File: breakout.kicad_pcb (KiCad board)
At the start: 2 copper layers, 26 x 23.8 mm, 11 parts, among them P1 CONN_01X09, P2 CONN_01X09, U1 ESP-12E, U2 APE8865Y5-33-HF-3

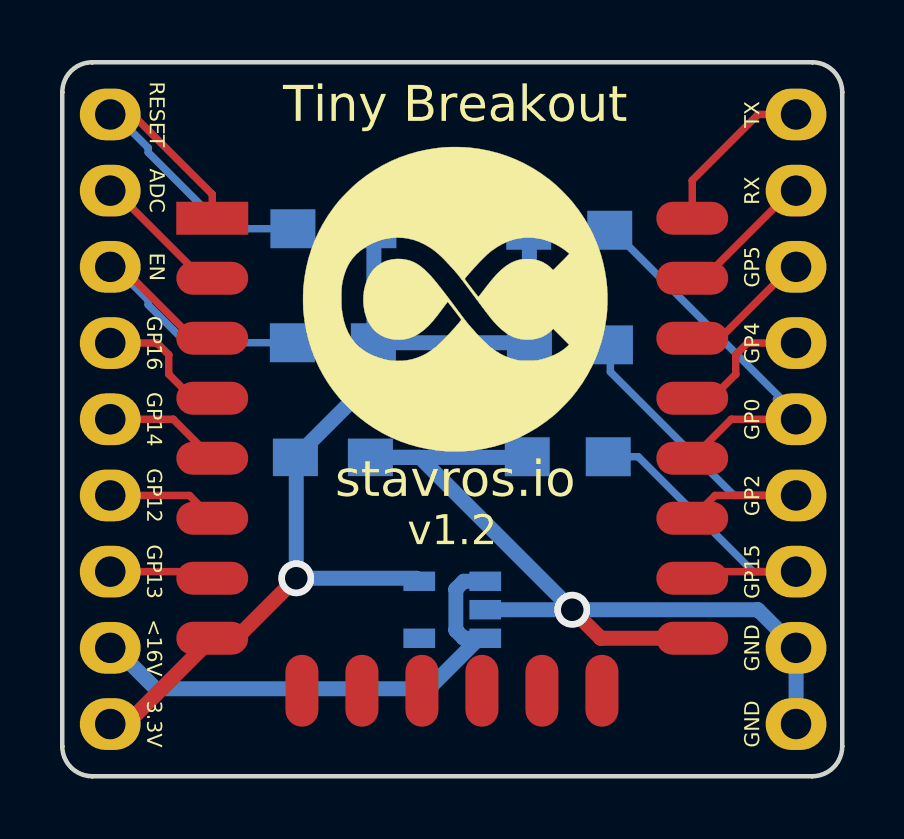
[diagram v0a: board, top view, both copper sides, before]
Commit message: Change to HT7333 regulator.
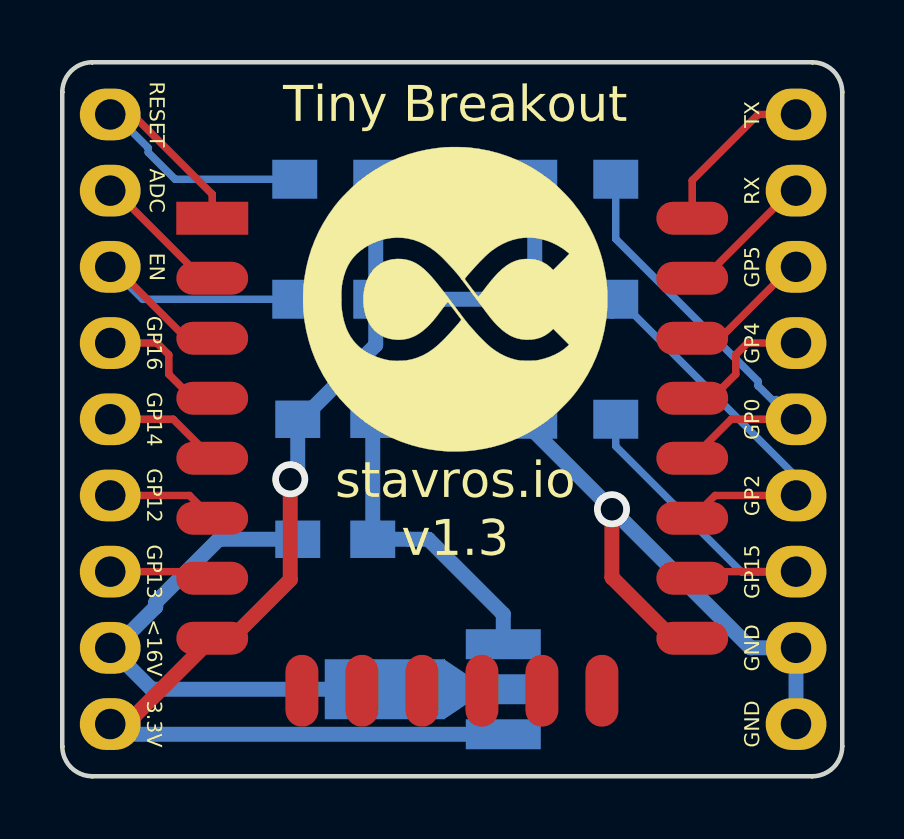
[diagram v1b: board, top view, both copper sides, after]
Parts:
- added C2: 10uF, Capacitors_SMD:C_0805_HandSoldering, B.Cu at (134.5, 67.5)
- C1: value 1uF -> 10uF
- U2: value APE8865Y5-33-HF-3 -> HT7333; footprint SOT-23-5 -> TO_SOT_Packages_SMD:SOT89-3_Housing_Handsoldering
- moved U2 2.73 mm to (137.8, 72.5), turned to 270 degrees
- moved R6 1.71 mm to (142.5, 55.5)
- moved R2 1.65 mm to (134.5, 55.5)
- moved R4 1.53 mm to (142.5, 59.5)
- moved R1 1.45 mm to (134.5, 59.5)
- moved R3 1.27 mm to (142.5, 63.5)
- moved C1 1.27 mm to (134.5, 63.5)
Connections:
- U2 pad 1: +12V -> GND
- U2 pad 2: GND -> /3V3
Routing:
- net /3V3: track 34.2 -> 50.4 mm
- net +12V: track 17.5 -> 23.1 mm
- net GND: track 31.9 -> 36.3 mm
- net Net-(P2-Pad5): track 13.9 -> 15.7 mm
- net Net-(P2-Pad7): track 11.4 -> 12.2 mm
- net Net-(P1-Pad1): track 13.1 -> 12.4 mm
- net Net-(P1-Pad3): track 11.6 -> 11.0 mm
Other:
- board text added: "stavros.io v1.3"
- board text removed: "C1"
- board text removed: "R1"
- board text removed: "R2"
- board text removed: "R3"
- board text removed: "R4"
- board text removed: "R6"
- board text removed: "stavros.io"
- board text removed: "v1.2"

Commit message: Switch back to the SPX regulator.
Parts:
- removed G***: LOGO, Stochastic:Logo_10mm
- U2: value HT7333 -> SPX3819M5-L-3-3; footprint TO_SOT_Packages_SMD:SOT89-3_Housing_Handsoldering -> TO_SOT_Packages_SMD:SOT-23-5
- moved U2 0.90 mm to (138.5, 72.0), turned to 180 degrees
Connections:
- U2 pad 1: GND -> +12V
- U2 pad 2: /3V3 -> GND
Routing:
- net GND: track 36.3 -> 43.8 mm
- net +12V: track 23.1 -> 19.2 mm
- net /3V3: track 50.4 -> 49.2 mm
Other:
- board text added: "stavros.io v1.4"
- board text removed: "stavros.io v1.3"

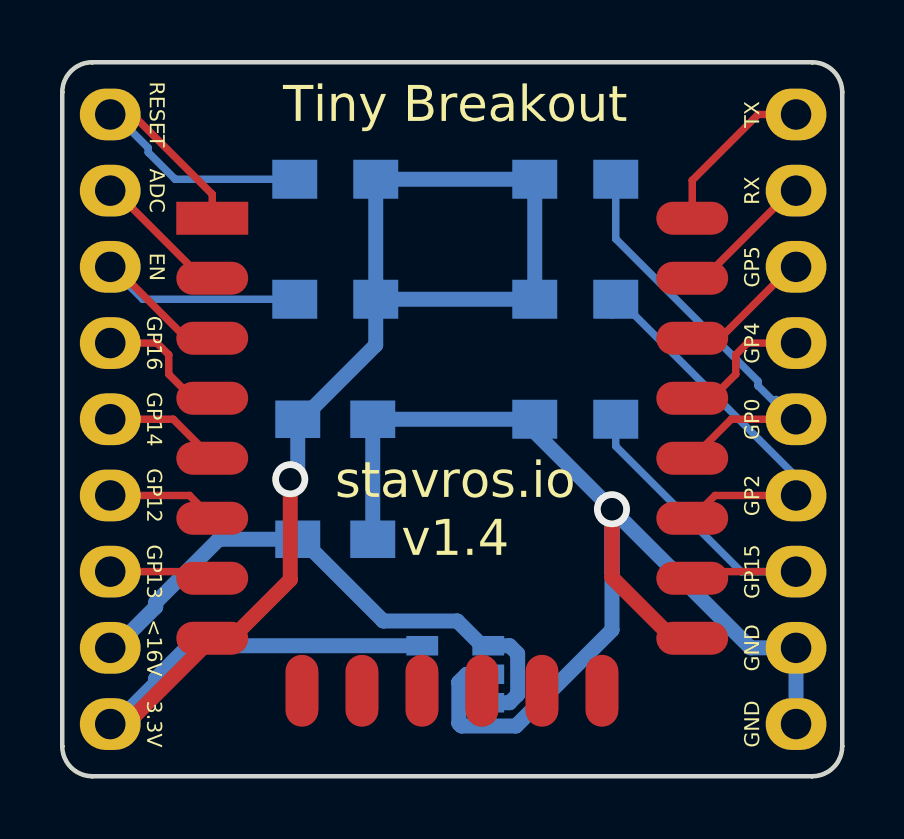
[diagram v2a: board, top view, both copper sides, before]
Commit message: Make PCB a bit smaller.
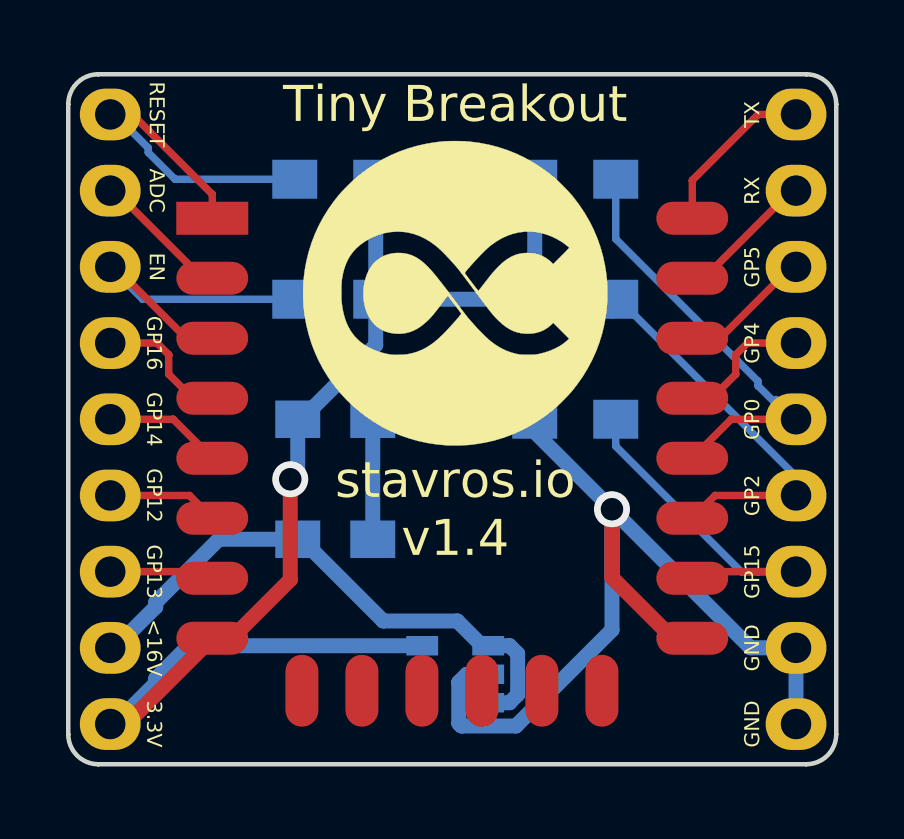
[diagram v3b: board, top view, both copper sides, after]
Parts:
- added G***: LOGO, Stochastic:Logo_10mm, F.Cu at (138.5, 59.3)
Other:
- board size 26 x 23.8 mm -> 25.6 x 23 mm

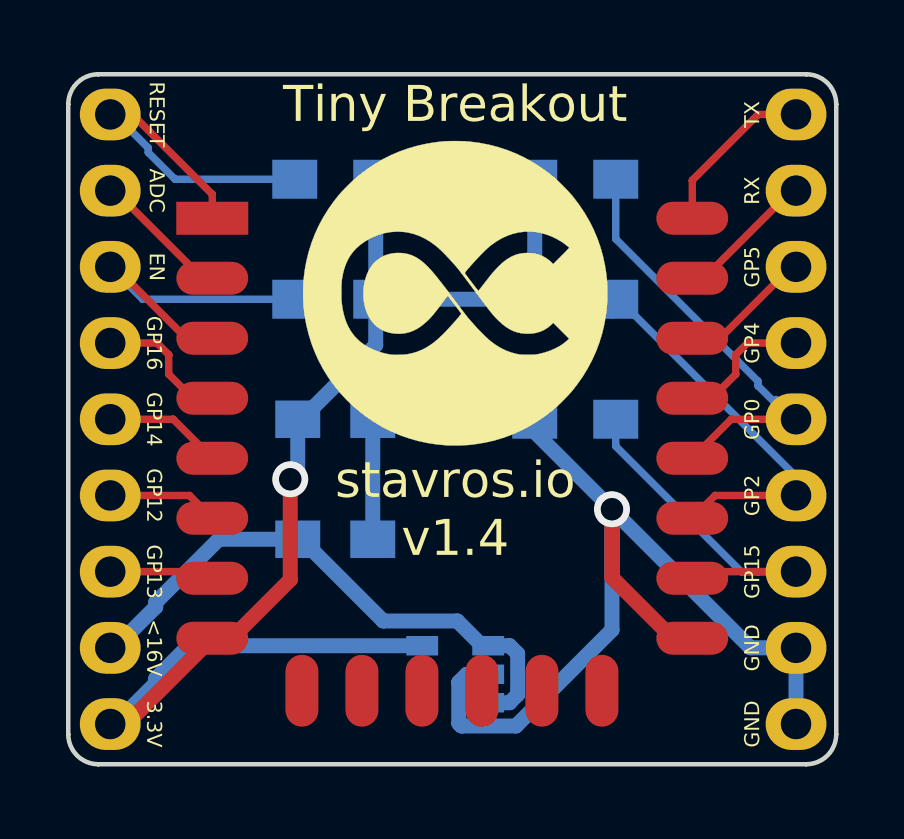
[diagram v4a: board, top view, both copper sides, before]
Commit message: Make an even tinier PCB
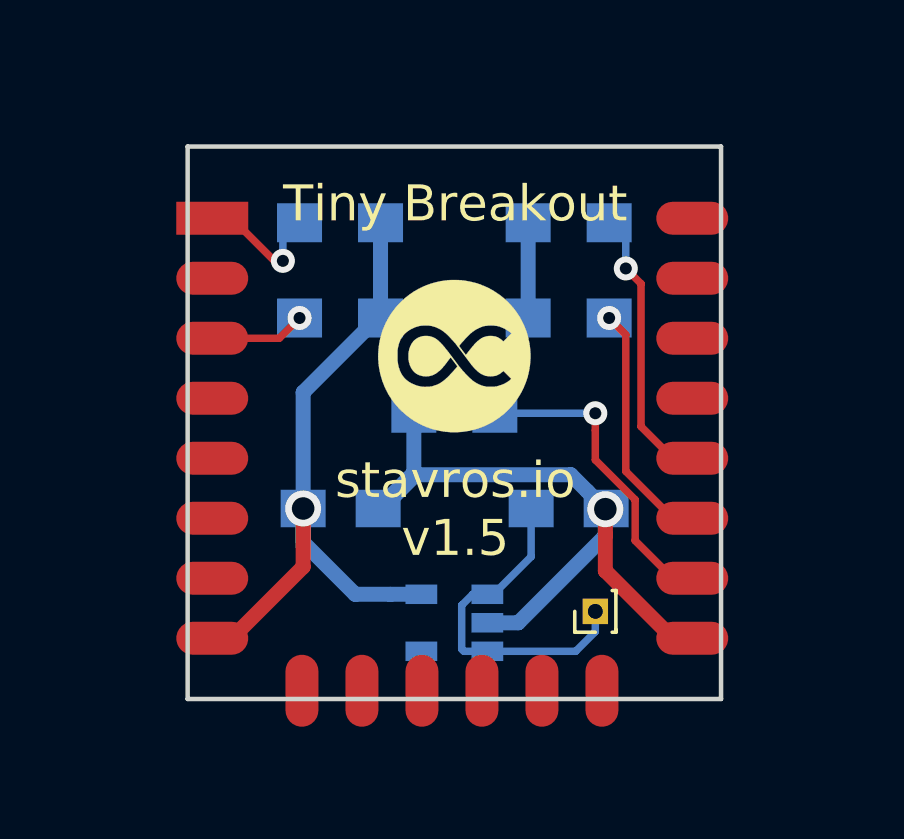
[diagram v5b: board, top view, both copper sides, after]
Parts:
- removed the G*** at (138.5, 59.3)
- removed P1, P2: CONN_01X09, Pin_Headers:Pin_Header_Straight_1x09
- added 5V: Conn_01x01, Pin_Headers:Pin_Header_Straight_1x01_Pitch1.00mm, F.Cu at (143.2, 69.9)
- added G***: LOGO, Stochastic:Logo_5mm, F.Cu at (138.5, 61.4)
- C1, C2: value 10uF -> 22uF
- moved C2 7.85 mm to (142.3, 66.5)
- moved R3 4.03 mm to (138.5, 63.3)
- moved C1 2.98 mm to (134.7, 66.5)
- moved U2 1.72 mm to (138.5, 70.3)
- moved R6 1.47 mm to (142.3, 57.0)
- moved R2 1.46 mm to (134.7, 57.0)
- moved R4 0.66 mm to (142.3, 60.1)
- moved R1 0.65 mm to (134.7, 60.1)
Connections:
- net +12V renamed +5V
- U1 pad 19: Net-(P2-Pad4) -> (no net)
- U1 pad 2: Net-(P1-Pad2) -> (no net)
- U1 pad 20: Net-(P2-Pad3) -> (no net)
- U1 pad 21: Net-(P2-Pad2) -> (no net)
- U1 pad 22: Net-(P2-Pad1) -> (no net)
- U1 pad 4: Net-(P1-Pad4) -> (no net)
- U1 pad 5: Net-(P1-Pad5) -> (no net)
- U1 pad 6: Net-(P1-Pad6) -> (no net)
- U1 pad 7: Net-(P1-Pad7) -> (no net)
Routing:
- net GND: track 43.8 -> 24.1 mm
- net /3V3: track 49.2 -> 31.8 mm
- net Net-(R2-Pad2): track 12.4 -> 4.44 mm, vias 0 -> 1
- net Net-(R1-Pad2): track 11.0 -> 3.19 mm, vias 0 -> 1
- net +5V: track 19.2 -> 11.5 mm
- net Net-(R6-Pad2): track 15.7 -> 9.38 mm, vias 0 -> 1
- net Net-(P2-Pad1): track 5.63 -> 0.00 mm
- net Net-(R4-Pad2): track 13.0 -> 8.20 mm, vias 0 -> 1
- net Net-(P2-Pad2): track 4.67 -> 0.00 mm
- net Net-(P1-Pad2): track 4.61 -> 0.00 mm
- net Net-(P2-Pad4): track 4.60 -> 0.00 mm
- net Net-(P1-Pad4): track 4.54 -> 0.00 mm
- net Net-(P2-Pad3): track 4.45 -> 0.00 mm
- net Net-(P1-Pad5): track 3.94 -> 0.00 mm
- net Net-(P1-Pad6): track 3.71 -> 0.00 mm
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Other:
- board size 25.6 x 23 mm -> 17.8 x 18.4 mm
- board text added: "stavros.io v1.5"
- board text removed: "stavros.io v1.4"

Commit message: Add images
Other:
- board text added: "Tinier Breakout"
- board text added: "stavros.io v1.0"
- board text removed: "Tiny Breakout"
- board text removed: "stavros.io v1.5"
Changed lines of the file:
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@@
     (effects (font (size 0.5 0.5) (thickness 0.125)) (justify right mirror))
   )
-  (gr_text "Tiny Breakout" (at 138.5 56.315) (layer F.SilkS)
+  (gr_text "Tinier Breakout" (at 138.5 56.315) (layer F.SilkS)
     (effects (font (size 1.2 1.2) (thickness 0.3)))
   )
-  (gr_text "stavros.io\nv1.5" (at 138.5 66.5) (layer F.SilkS)
+  (gr_text "stavros.io\nv1.0" (at 138.5 66.5) (layer F.SilkS)
     (effects (font (size 1.2 1.2) (thickness 0.3)))
   )

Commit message: Improve text
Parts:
- renumbered R1 to 10kΩ, R2 to 10kΩ, R3 to 10kΩ, R4 to 10kΩ, R6 to 10kΩ, C1 to 22uF, C2 to 22uF
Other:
- board size 17.8 x 18.4 mm -> 17.8 x 19.1 mm
- board text added: "LDO"
- board text added: "RST"
- board text removed: "RESET"
- board text removed: "VR"
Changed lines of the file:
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@@
     (links 18)
     (no_connects 0)
-    (area 129.504999 54.334999 147.435001 72.900001)
+    (area 129.464999 53.899999 147.395001 73.100001)
     (thickness 1.6)
-    (drawings 24)
+    (drawings 28)
     (tracks 71)
     (zones 0)
@@
     (tags "capacitor 0805")
     (attr smd)
-    (fp_text reference C1 (at -0.02 -1.524) (layer B.SilkS)
+    (fp_text reference 22uF (at -0.02 -1.524) (layer B.SilkS)
       (effects (font (size 0.75 0.75) (thickness 0.1875)) (justify mirror))
     )
@@
     (tags "resistor 0805")
     (attr smd)
-    (fp_text reference R1 (at 0 1.524 180) (layer B.SilkS)
+    (fp_text reference 10kΩ (at 0 1.524 180) (layer B.SilkS)
       (effects (font (size 0.75 0.75) (thickness 0.1875)) (justify mirror))
     )
@@
     (tags "resistor 0805")
     (attr smd)
-    (fp_text reference R2 (at 0 1.524 180) (layer B.SilkS)
+    (fp_text reference 10kΩ (at 0 1.524 180) (layer B.SilkS)
       (effects (font (size 0.75 0.75) (thickness 0.1875)) (justify mirror))
     )
@@
     (tags "resistor 0805")
     (attr smd)
-    (fp_text reference R3 (at 0 1.524 180) (layer B.SilkS)
+    (fp_text reference 10kΩ (at 0 1.524 180) (layer B.SilkS)
       (effects (font (size 0.75 0.75) (thickness 0.1875)) (justify mirror))
     )
@@
     (tags "resistor 0805")
     (attr smd)
-    (fp_text reference R4 (at 0 -1.524) (layer B.SilkS)
+    (fp_text reference 10kΩ (at 0 -1.524) (layer B.SilkS)
       (effects (font (size 0.75 0.75) (thickness 0.1875)) (justify mirror))
     )
@@
     (tags "resistor 0805")
     (attr smd)
-    (fp_text reference R6 (at 0 -1.524) (layer B.SilkS)
+    (fp_text reference 10kΩ (at 0 -1.524) (layer B.SilkS)
       (effects (font (size 0.75 0.75) (thickness 0.1875)) (justify mirror))
     )
@@
     (tags "capacitor 0805")
     (attr smd)
-    (fp_text reference C2 (at 0 1.524 180) (layer B.SilkS)
+    (fp_text reference 22uF (at 0 1.524 180) (layer B.SilkS)
       (effects (font (size 0.75 0.75) (thickness 0.1875)) (justify mirror))
     )
@@
     )
   )
-  (gr_line (start 147.36 54.41) (end 147.36 72.825) (layer Edge.Cuts) (width 0.15))
+  (gr_arc (start 146.05 71.755) (end 147.32 71.755) (angle 90) (layer Edge.Cuts) (width 0.15))
+  (gr_arc (start 130.81 71.755) (end 130.81 73.025) (angle 90) (layer Edge.Cuts) (width 0.15))
+  (gr_arc (start 130.81 55.245) (end 129.54 55.245) (angle 90) (layer Edge.Cuts) (width 0.15))
+  (gr_arc (start 146.05 55.245) (end 146.05 53.975) (angle 90) (layer Edge.Cuts) (width 0.15))
+  (gr_line (start 147.32 55.245) (end 147.32 71.755) (layer Edge.Cuts) (width 0.15))
   (gr_text 3.3V (at 130.215 70.92) (layer B.SilkS)
     (effects (font (size 0.5 0.5) (thickness 0.125)) (justify right mirror))
@@
     (effects (font (size 0.5 0.5) (thickness 0.125)) (justify left mirror))
   )
-  (gr_text RESET (at 130.215 56.95) (layer B.SilkS)
+  (gr_text RST (at 130.215 56.95) (layer B.SilkS)
     (effects (font (size 0.5 0.5) (thickness 0.125)) (justify right mirror))
   )
@@
     (effects (font (size 0.5 0.5) (thickness 0.125)) (justify mirror))
   )
-  (gr_text VR (at 138.5 67.872) (layer B.SilkS)
+  (gr_text LDO (at 138.5 67.872) (layer B.SilkS)
     (effects (font (size 0.75 0.75) (thickness 0.1875)) (justify mirror))
   )
-  (gr_line (start 129.58 72.825) (end 129.58 54.41) (layer Edge.Cuts) (width 0.15))
-  (gr_line (start 147.36 72.825) (end 129.58 72.825) (layer Edge.Cuts) (width 0.15))
-  (gr_line (start 129.58 54.41) (end 147.36 54.41) (layer Edge.Cuts) (width 0.15))
+  (gr_line (start 129.54 71.755) (end 129.54 55.245) (layer Edge.Cuts) (width 0.15))
+  (gr_line (start 146.05 73.025) (end 130.81 73.025) (layer Edge.Cuts) (width 0.15))
+  (gr_line (start 130.81 53.975) (end 146.05 53.975) (layer Edge.Cuts) (width 0.15))
   (segment (start 143.502676 67.345777) (end 143.502676 66.497249) (width 0.5) (layer B.Cu) (net 1))
   (segment (start 139.57 70.285) (end 140.6 70.285) (width 0.5) (layer B.Cu) (net 1))
